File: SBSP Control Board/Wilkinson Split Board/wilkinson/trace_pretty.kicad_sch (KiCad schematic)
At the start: 66 parts, among them IC1 SN74AVC2T245RSWR, J1 Conn_01x02_Socket, J10 Conn_Coaxial, J11 Conn_Coaxial, J12 Conn_Coaxial, J13 Conn_Coaxial, J14 Conn_Coaxial, J15 Conn_Coaxial, J2 Conn_01x02_Socket, J3 Conn_01x20_Socket, J4 Conn_01x20_Socket, J5 Conn_01x02_Pin, J6 Conn_01x02_Pin, J7 Conn_01x02_Pin, J8 Conn_Coaxial, J9 Conn_Coaxial, U1 ADAR1000ACCZN, U2 SN74AVC4T245PW, U3 SN74AVC4T245PW

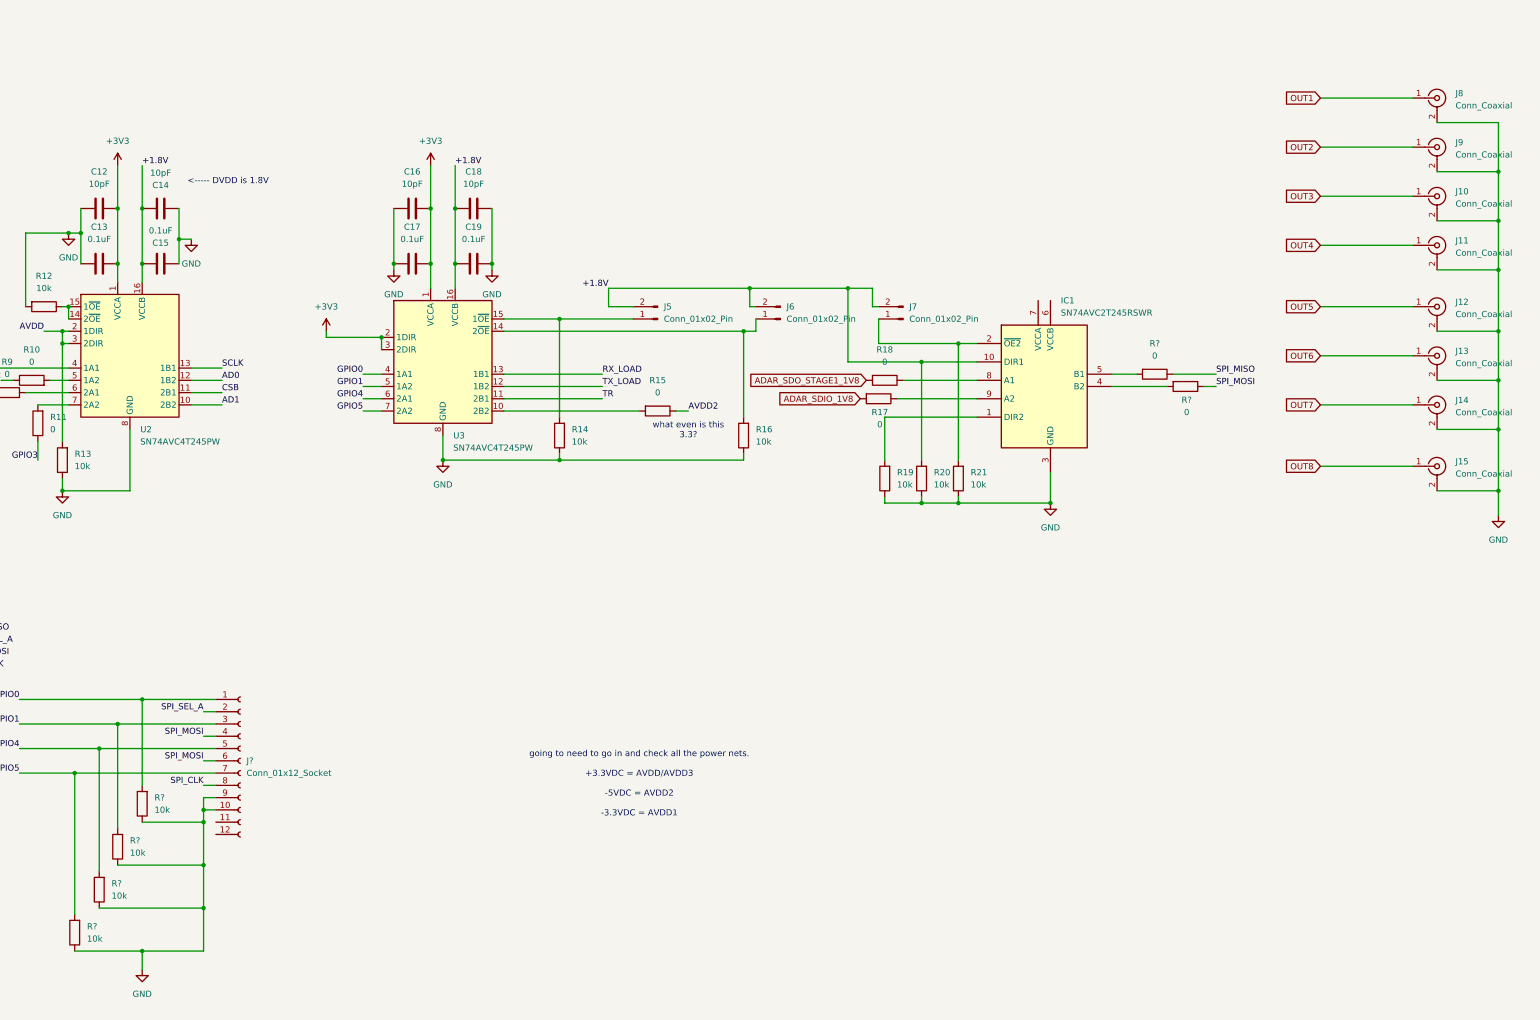
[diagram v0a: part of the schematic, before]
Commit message: fixed routing
monday: 5 hrs: talked to fayed about what exactly we needed to do, emailed fathy about what we do, get approval, re do schematic and layout to get wilkinson layout started. started workin on new schematic, started creating the adar1000 footprint and sch symbol, re did board outline and got traces from xmicrowave board, started doing layout for adar supporting passive components.

tuesday, 3 hrs (12-3), worked on adding level shifting circuit and began designing schematic for level shifting and ensuring each power level was correct and the schematic was equal in function to the evaluation board schematic.

wednesday: 5 (10-3), further schematic work, finished schematic, and then began layout for board. got wilkinson geometry from fayed and began its implementation into the design. layout is not done yet, but should not take much longer.

thursday: 5 (10-3)more layout work on the schematic, finished the level shifting circuit and added the power side to the layout and circuit.
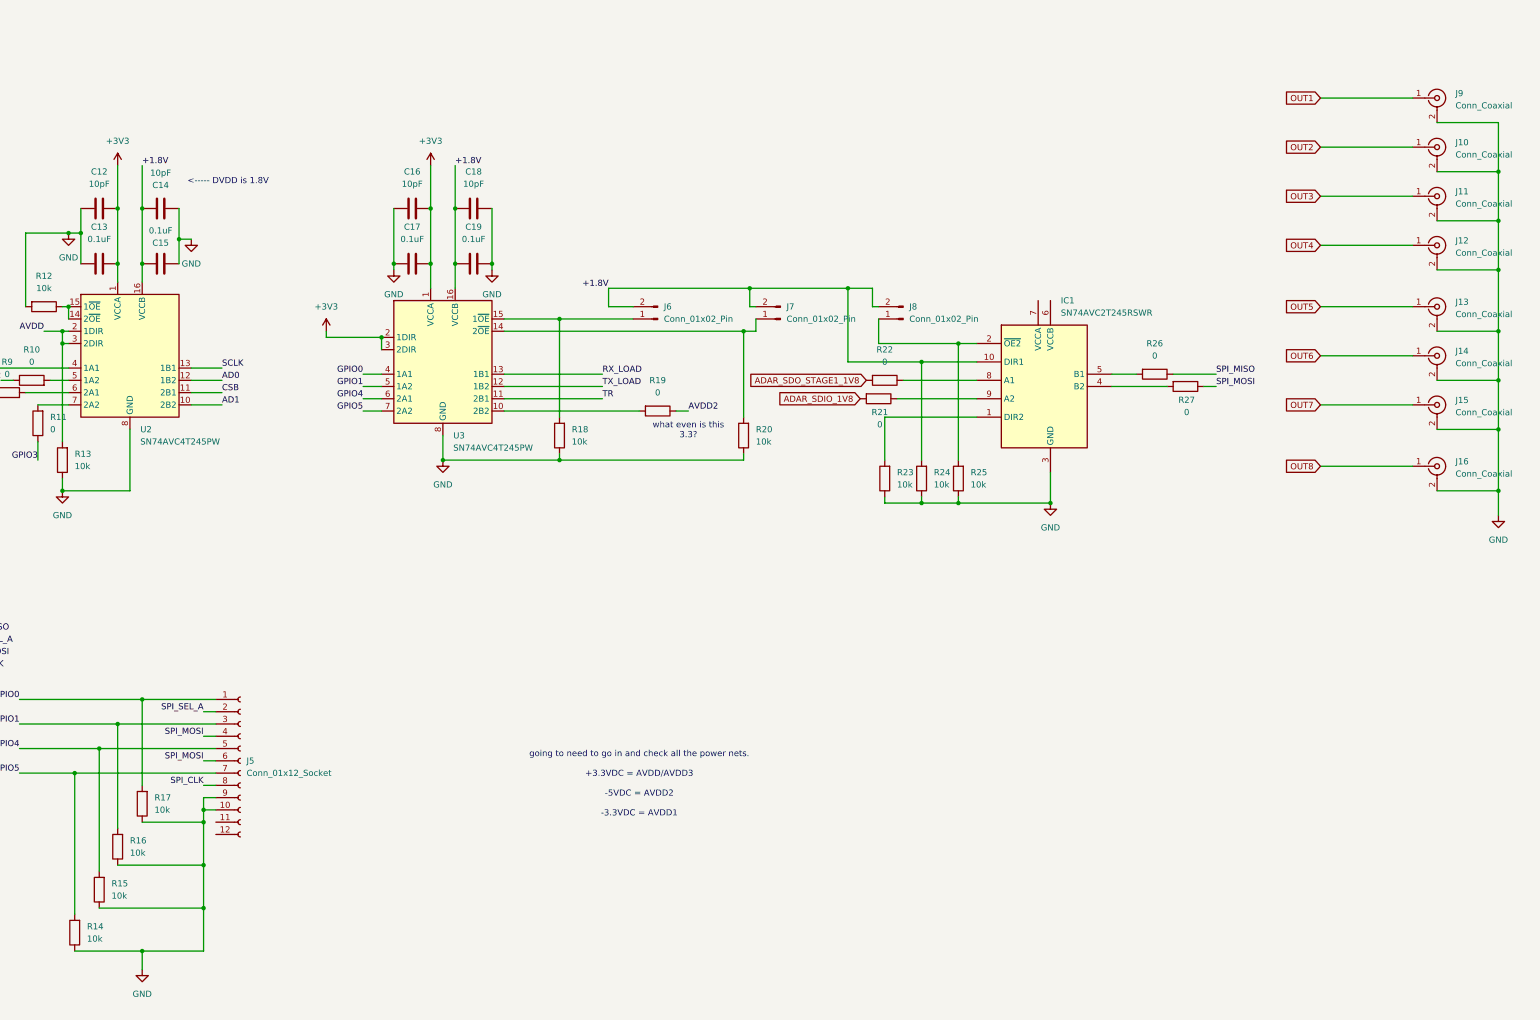
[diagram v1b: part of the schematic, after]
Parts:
- gave numbers to parts that had none: 7
- renumbered J9 to J10, J10 to J11, J11 to J12, J12 to J13, J13 to J14, J14 to J15, J15 to J16, J5 to J6, J6 to J7, J7 to J8, J8 to J9, R14 to R18, R15 to R19, R16 to R20, R17 to R21, R18 to R22, R19 to R23, R20 to R24, R21 to R25

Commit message: added wilkinson geometry
11:00 to 3:00

learned from nolan how the thing works and how to run and use it/test it. I then worked on the control circuit testing and wrote report on it. individually tested every patch to ensure the values matched the MATLAB sims. this took about 2 hours. the next two hours was spent working on the 1-8 splitter board. I finished adding the wilkinson geometry onto the board and began laying out the passive components.
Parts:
- added J20: Conn_Coaxial, Connector_Coaxial:SMA_Amphenol_132289_EdgeMount, symbol Connector:Conn_Coaxial
- added R45: 100, Resistor_SMD:R_0402_1005Metric, symbol Device:R
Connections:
- net GND: now also J20.2 (Ext)
- net PLL_IN: now also J20.1 (In), R45.1, R45.2
